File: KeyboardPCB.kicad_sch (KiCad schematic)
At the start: 12 parts, among them J1 AVR-ISP-6, U1 ATmega32U4-A, Y1 Crystal_GND24_Small

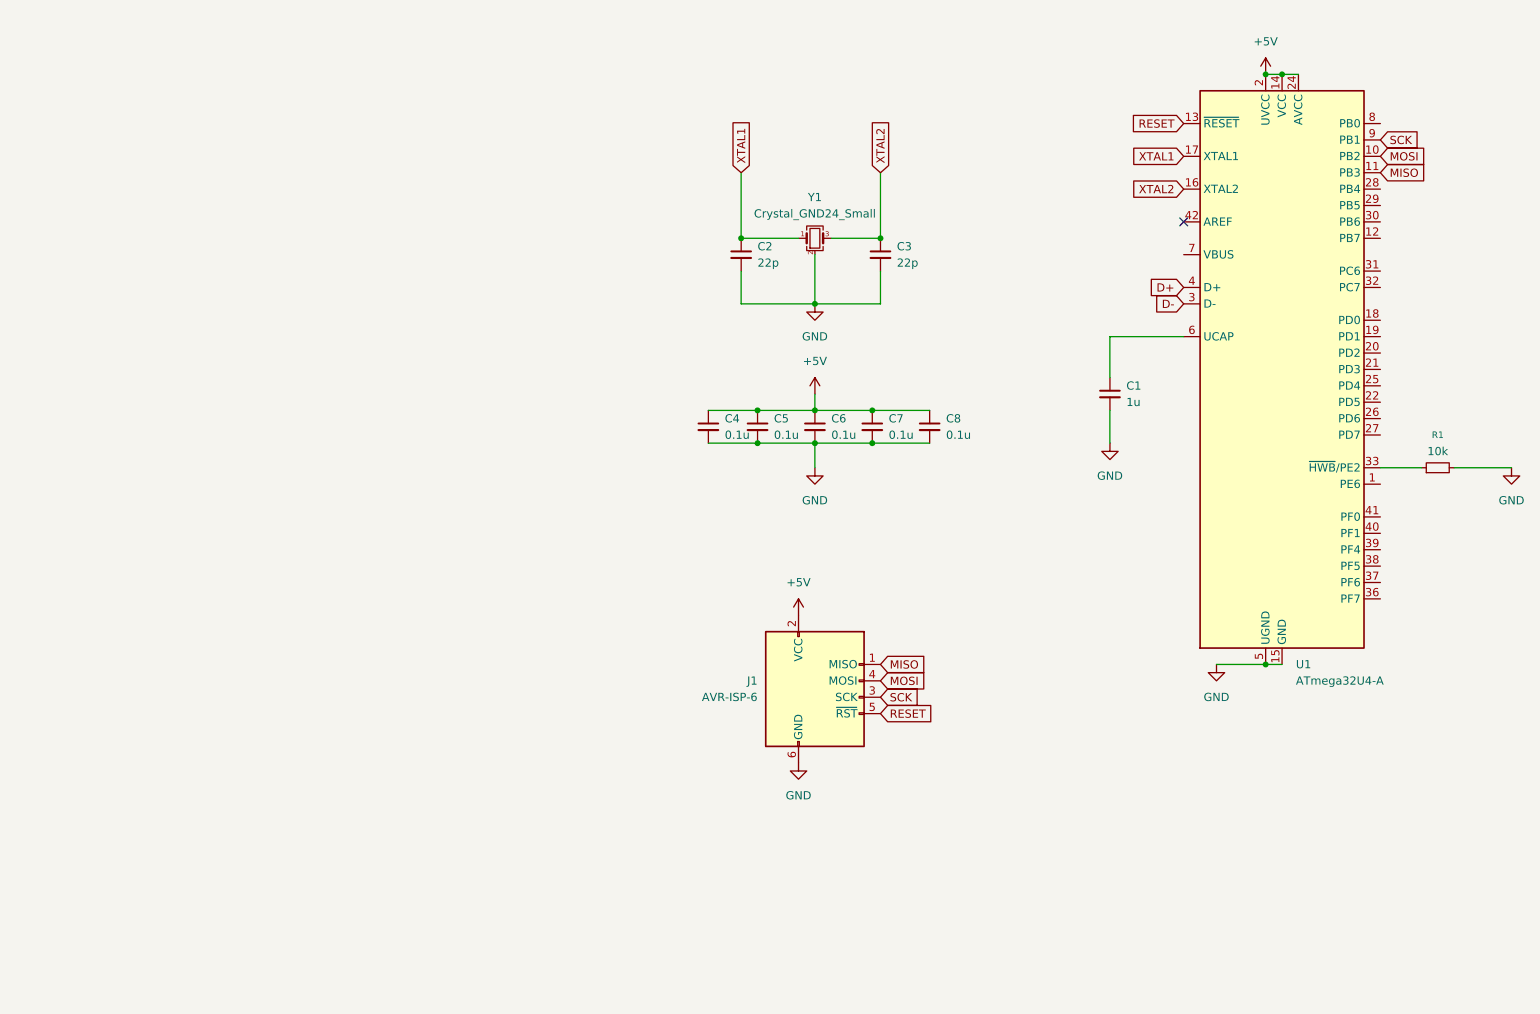
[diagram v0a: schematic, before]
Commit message: Major progress
- Schematic Finished
- Footprints applied
- Working on PCB now
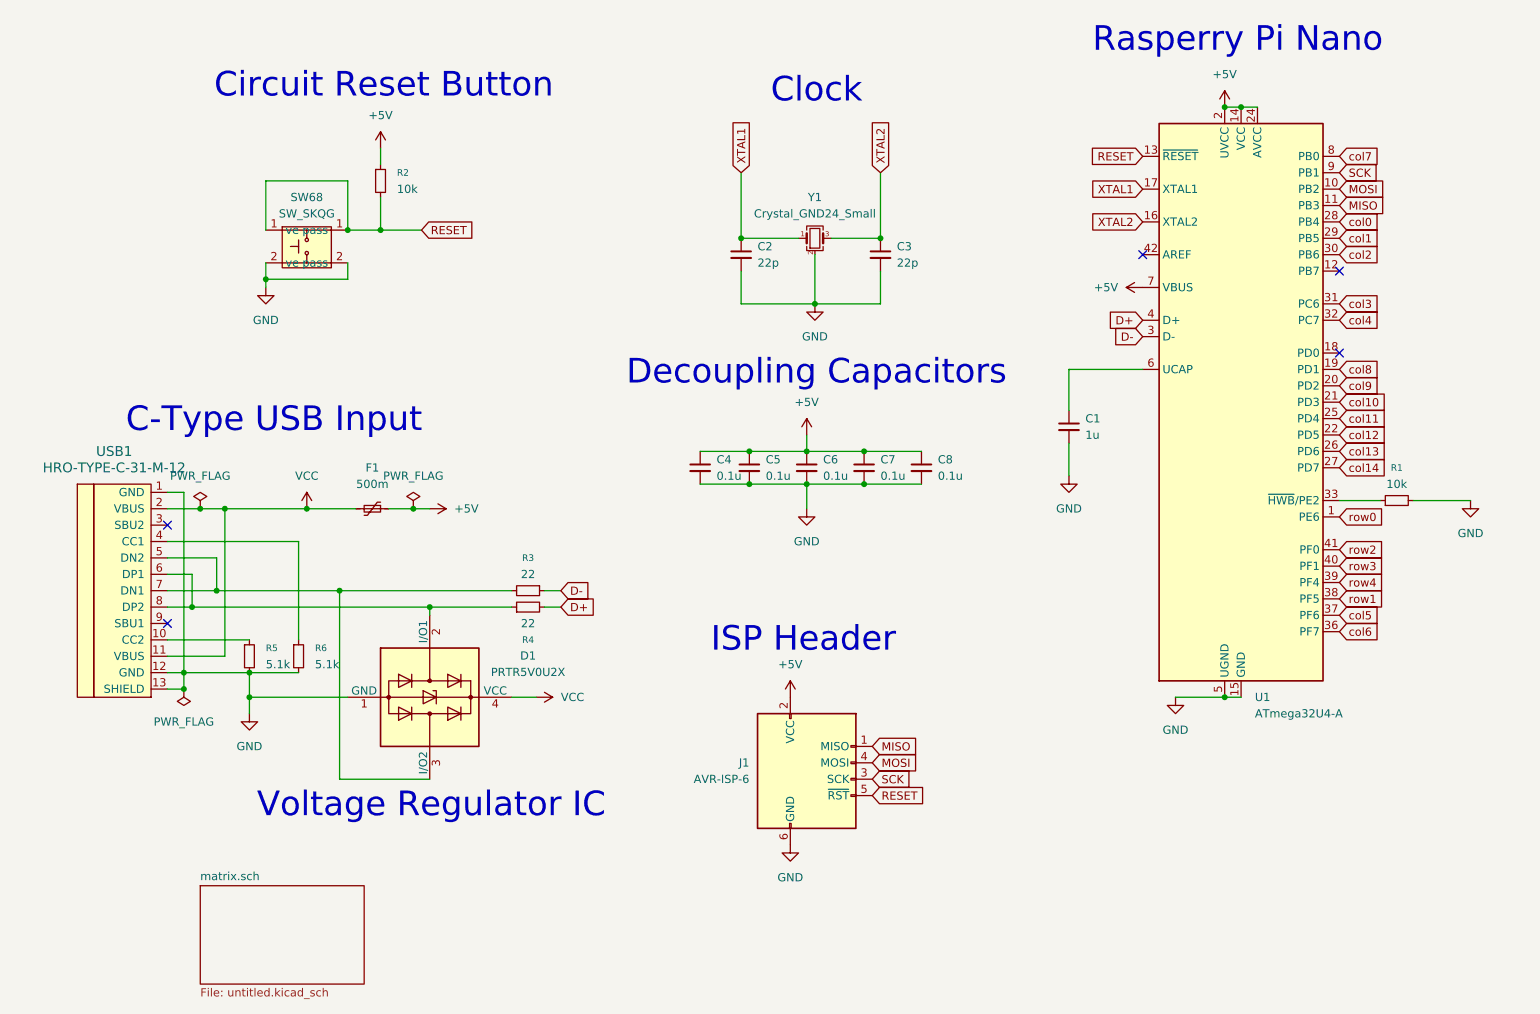
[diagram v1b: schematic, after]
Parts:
- added D1: PRTR5V0U2X, Diode_SMD:D_SOD-123, symbol Power_Protection:PRTR5V0U2X
- added F1: 500m, Fuse:Fuse_1206_3216Metric_Pad1.42x1.75mm_HandSolder, symbol Device:Polyfuse_Small
- added R2: 10k, Resistor_SMD:R_0805_2012Metric_Pad1.20x1.40mm_HandSolder, symbol Device:R_Small
- added R3, R4: 22, Resistor_SMD:R_0805_2012Metric_Pad1.20x1.40mm_HandSolder, symbol Device:R_Small
- added R5, R6: 5.1k, Resistor_SMD:R_0805_2012Metric_Pad1.20x1.40mm_HandSolder, symbol Device:R_Small
- added SW68: SW_SKQG, Button_Switch_SMD:SW_SPST_SKQG_WithStem, symbol local:SW_SKQG
- added USB1: HRO-TYPE-C-31-M-12, Type-C:HRO-TYPE-C-31-M-12-HandSoldering, symbol Type-C:HRO-TYPE-C-31-M-12
- C1, C2, C3, C4, C5, C6, C7: footprint (none) -> Capacitor_SMD:C_0805_2012Metric
- C8: footprint (none) -> Diode_SMD:D_SOD-123
- J1: footprint (none) -> random-keyboard-parts:D_SOD-123-Pretty
- R1: footprint (none) -> Resistor_SMD:R_0805_2012Metric_Pad1.20x1.40mm_HandSolder
- Y1: footprint (none) -> Crystal:Crystal_SMD_3225-4Pin_3.2x2.5mm
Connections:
- net +5V: now also U1.7 (VBUS), F1.1, R2.1
- net D+: now also R4.2
- net D-: now also R3.1
- net GND: now also D1.1 (GND), R5.2, R6.2, SW68.2 (pass), USB1.1 (GND), USB1.12 (GND), USB1.13 (SHIELD)
- net RESET: now also R2.2, SW68.1 (pass)
- net row0: now reaches U1.1 (PE6)
- net col8: now reaches U1.19 (PD1)
- net col9: now reaches U1.20 (PD2)
- net col10: now reaches U1.21 (PD3)
- net col12: now reaches U1.22 (PD5)
- net col11: now reaches U1.25 (PD4)
- net col13: now reaches U1.26 (PD6)
- net col14: now reaches U1.27 (PD7)
- net col0: now reaches U1.28 (PB4)
- net col1: now reaches U1.29 (PB5)
- net col2: now reaches U1.30 (PB6)
- net col3: now reaches U1.31 (PC6)
- net col4: now reaches U1.32 (PC7)
- net col6: now reaches U1.36 (PF7)
- net col5: now reaches U1.37 (PF6)
- net row1: now reaches U1.38 (PF5)
- net row4: now reaches U1.39 (PF4)
- net row3: now reaches U1.40 (PF1)
- net row2: now reaches U1.41 (PF0)
- net col7: now reaches U1.8 (PB0)
- new net: D1.3 (I/O2), R3.2, USB1.5 (DN2), USB1.7 (DN1)
- new net: D1.2 (I/O1), R4.1, USB1.6 (DP1), USB1.8 (DP2)
- new net: R5.1, USB1.10 (CC2)
- new net: R6.1, USB1.4 (CC1)
- new net VCC: D1.4 (VCC), F1.2, USB1.11 (VBUS), USB1.2 (VBUS)
- no-connect marks 1 -> 5
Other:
- added sheet matrix.sch (untitled.kicad_sch)
- note added: "C-Type USB Input"
- note added: "Circuit Reset Button"
- note added: "Clock"
- note added: "Decoupling Capacitors"
- note added: "ISP Header"
- note added: "Rasperry Pi Nano"
- note added: "Voltage Regulator IC"
- company: (none) -> Landon Wardle
- title: (none) -> Master Zen Keyboard PCB
- moved on the sheet: C1, C4, C5, C6, C7, C8, J1, R1, U1

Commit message: Keyboard keys positioned
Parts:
- D1: footprint Diode_SMD:D_SOD-123 -> random-keyboard-parts:SOT143B
- J1: footprint random-keyboard-parts:D_SOD-123-Pretty -> random-keyboard-parts:Reset_Pretty-Mask
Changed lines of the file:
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@@
 			)
 		)
-		(property "Footprint" "Diode_SMD:D_SOD-123"
+		(property "Footprint" "random-keyboard-parts:SOT143B"
 			(at 111.76 133.604 0)
 			(hide yes)
@@
 			)
 		)
-		(property "Footprint" "random-keyboard-parts:D_SOD-123-Pretty"
+		(property "Footprint" "random-keyboard-parts:Reset_Pretty-Mask"
 			(at 163.83 143.51 90)
 			(hide yes)

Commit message: Layout progress.
Moved the diodes to each of their keys.
Mostly finished placing capacitors, resistors, and other components.
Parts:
- renumbered D1 to D0
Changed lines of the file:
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@@
 		(dnp no)
 		(fields_autoplaced yes)
-		(property "Reference" "D1"
+		(property "Reference" "D0"
 			(at 127 125.6598 90)
 			(show_name no)
@@
 			(project "KeyboardPCB"
 				(path "/fcb3ea0f-2b01-4294-acd9-14d7363b0fdb"
-					(reference "D1")
+					(reference "D0")
 					(unit 1)
 				)

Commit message: PCB Layout finished.
Placed all components on the board.
Figured out where all the decoupling capacitors go!
Also fixed an issue with one of the decoupling capacitors not being 10 uF.
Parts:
- C8: value 0.1u -> 10u; footprint Diode_SMD:D_SOD-123 -> Capacitor_SMD:C_0805_2012Metric
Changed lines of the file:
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@@
 			)
 		)
-		(property "Value" "0.1u"
+		(property "Value" "10u"
 			(at 190.5 97.7962 0)
 			(show_name no)
@@
 			)
 		)
-		(property "Footprint" "Diode_SMD:D_SOD-123"
+		(property "Footprint" "Capacitor_SMD:C_0805_2012Metric"
 			(at 187.96 96.52 0)
 			(hide yes)

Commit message: Routed about half of the PCB
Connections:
- net DN: now reaches D0.3 (I/O2), R3.2, USB1.5 (DN2), USB1.7 (DN1)
- net DP: now reaches D0.2 (I/O1), R4.1, USB1.6 (DP1), USB1.8 (DP2)
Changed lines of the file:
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@@
+		)
+	)
+	(global_label "DP"
+		(shape input)
+		(at 87.63 118.11 270)
+		(fields_autoplaced yes)
+		(effects
+			(font
+				(size 1.27 1.27)
+			)
+			(justify right)
+		)
+		(property "Intersheetrefs" "${INTERSHEET_REFS}"
+			(at 87.63 123.9376 90)
+			(hide yes)
+			(show_name no)
+			(do_not_autoplace no)
+			(effects
+				(font
+					(size 1.27 1.27)
+				)
+				(justify right)
+			)
 		)
 	)
@@
 			(hide yes)
 			(show_name no)
+			(do_not_autoplace no)
+			(effects
+				(font
+					(size 1.27 1.27)
+				)
+				(justify left)
+			)
+		)
+	)
+	(global_label "DN"
+		(shape input)
+		(at 87.63 115.57 90)
+		(fields_autoplaced yes)
+		(effects
+			(font
+				(size 1.27 1.27)
+			)
+			(justify left)
+		)
+		(property "Intersheetrefs" "${INTERSHEET_REFS}"
+			(at 87.63 109.9843 90)
+			(hide yes)
+			(show_name no)

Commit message: Continued routing
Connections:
- net col6: now also U1.38 (PF5); no longer U1.36 (PF7)
- net row0: now also U1.39 (PF4); no longer U1.1 (PE6)
- net row1: now also U1.40 (PF1); no longer U1.38 (PF5)
- net row3: now also U1.1 (PE6); no longer U1.40 (PF1)
- net row4: now also U1.36 (PF7); no longer U1.39 (PF4)
